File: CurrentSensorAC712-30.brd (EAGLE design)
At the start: 24 x 32 mm, 8 parts, among them U1 ACS712ELCTR30AT

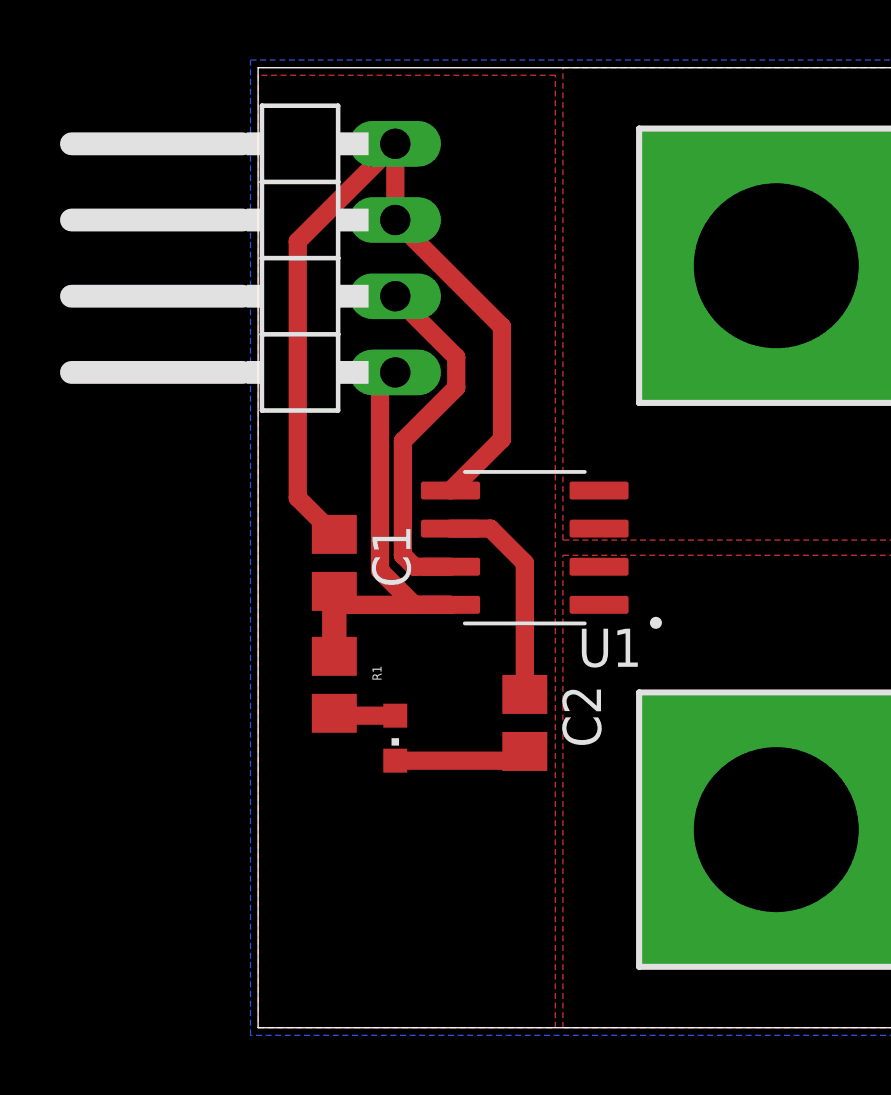
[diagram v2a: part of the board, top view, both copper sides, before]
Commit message: isolation distance improved
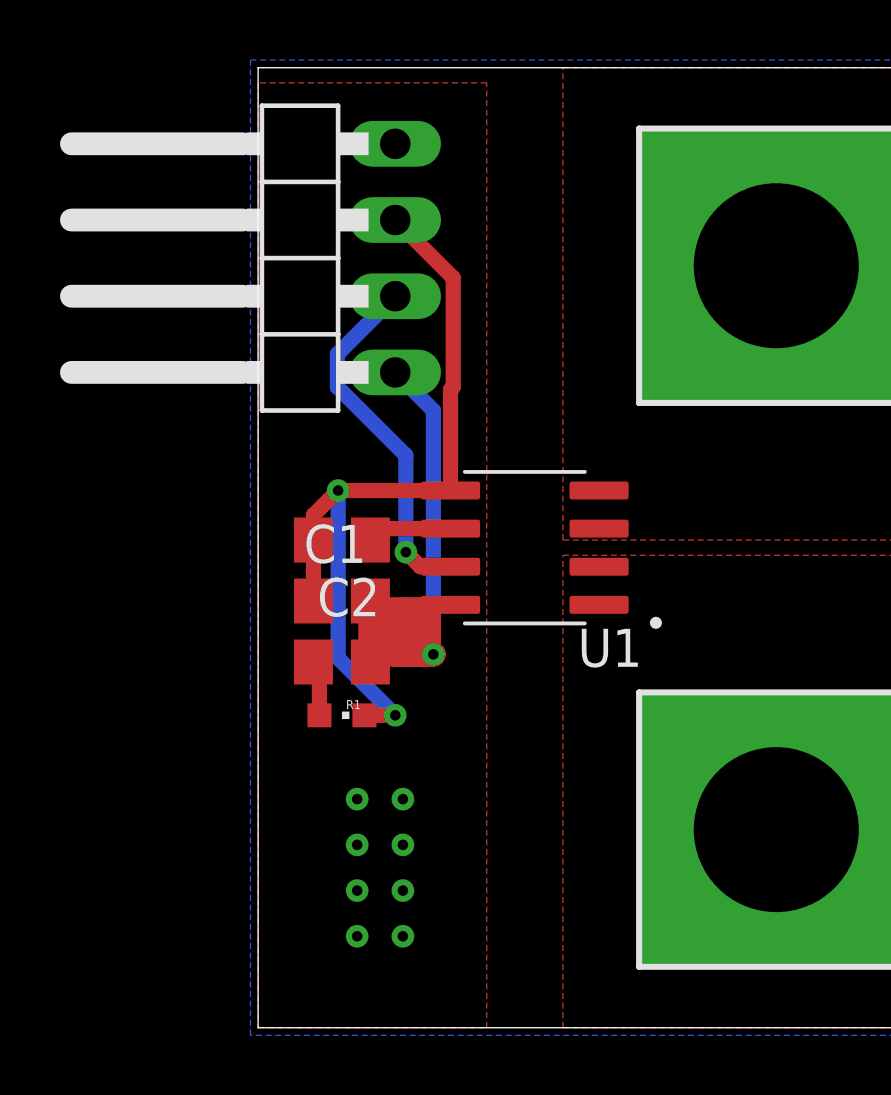
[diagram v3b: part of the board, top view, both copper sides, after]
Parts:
- moved C2 8.62 mm to (2.79, 16.3), turned to 180 degrees
- moved LED1 1.93 mm to (2.79, 10.4), turned to 270 degrees
- moved C1 1.30 mm to (2.79, 14.2), turned to 0 degrees
- moved R1 0.80 mm to (2.79, 12.2), turned to 180 degrees
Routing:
- net 5VDC: track 15.9 -> 33.3 mm, vias 0 -> 1
- net GND: track 33.1 -> 26.9 mm, vias 0 -> 10
- net N$4: track 7.33 -> 2.83 mm
- net N$6: vias 0 -> 1

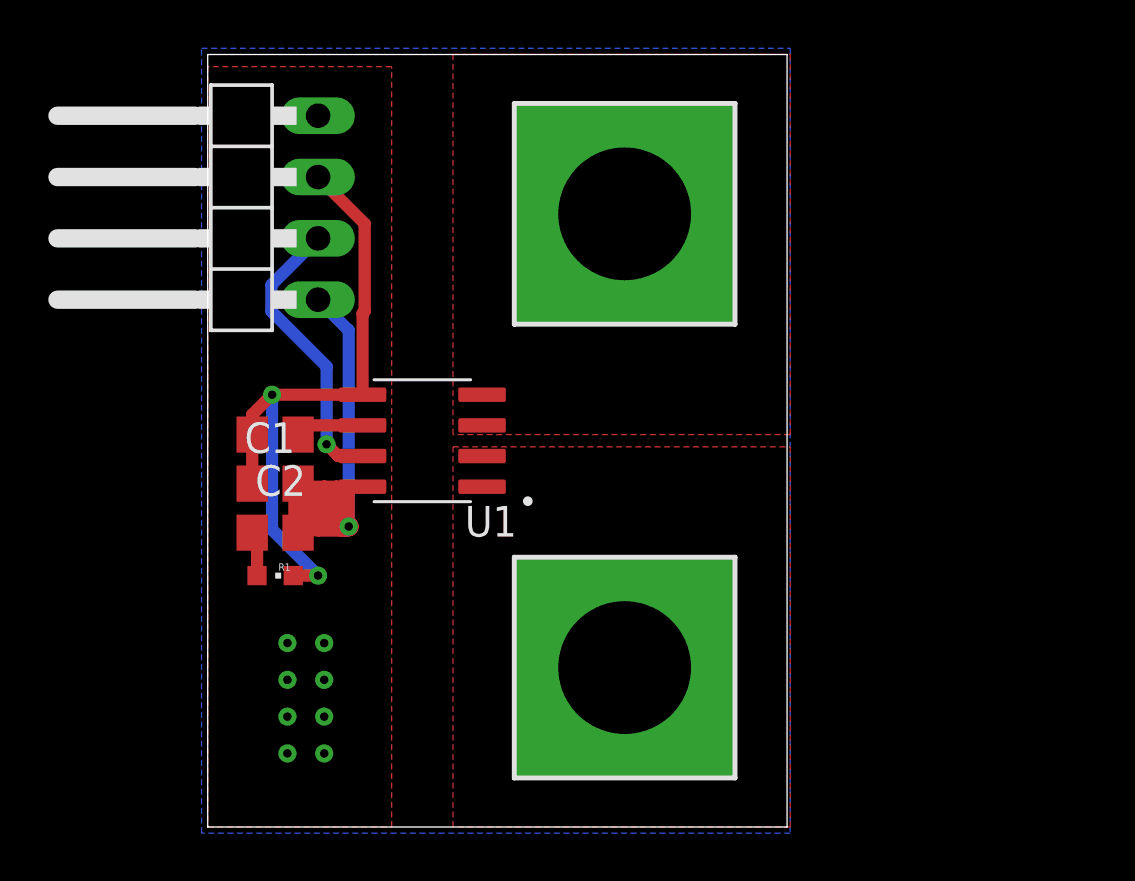
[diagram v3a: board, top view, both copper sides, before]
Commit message: new extension board design used
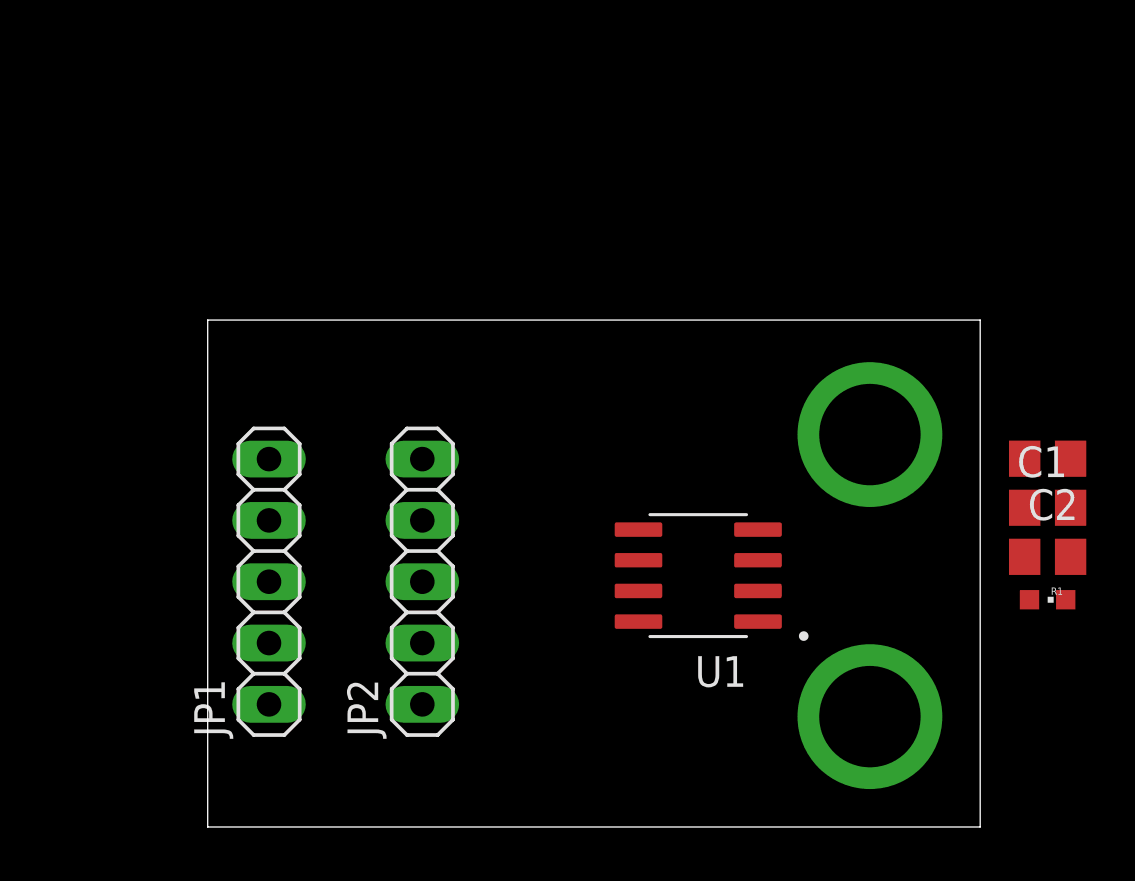
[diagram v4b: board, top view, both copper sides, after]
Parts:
- removed H1, H2: MOUNT-PAD-SQUARE5.5, holes:5,5-PAD-SQUARE
- added JP2: (no value), pinhead:1X05
- JP1: device pinhead:1X04/90 -> pinhead:1X05
- moved C1 32.0 mm to (34.8, 13.2)
- moved C2 32.0 mm to (34.8, 15.3)
- moved LED1 32.0 mm to (34.8, 9.41)
- moved R1 32.0 mm to (34.8, 11.2)
- moved JP1 15.6 mm to (2.54, 10.2)
- moved U1 12.7 mm to (20.3, 10.4)
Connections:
- net 5VDC: now also JP1.2
- net GND: now also JP1.5; no longer JP1.3
- net IN: no longer H1.B5,5
- net N$6: now also JP1.3; no longer JP1.2
- net OUT: no longer H2.B5,5
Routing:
- net 5VDC: track 33.3 -> 0.00 mm, vias 1 -> 0
- net GND: track 26.9 -> 0.00 mm, vias 10 -> 0
- net N$6: track 12.0 -> 0.00 mm, vias 1 -> 0
- net N$4: track 2.83 -> 0.00 mm
- net N$5: track 1.86 -> 0.00 mm
- removed copper zone on layer 1, net GND
- removed copper zone on layer 16, net GND
- removed copper zone on layer 1, net IN
- removed copper zone on layer 1, net OUT
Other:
- board size 24 x 32 mm -> 32 x 21 mm

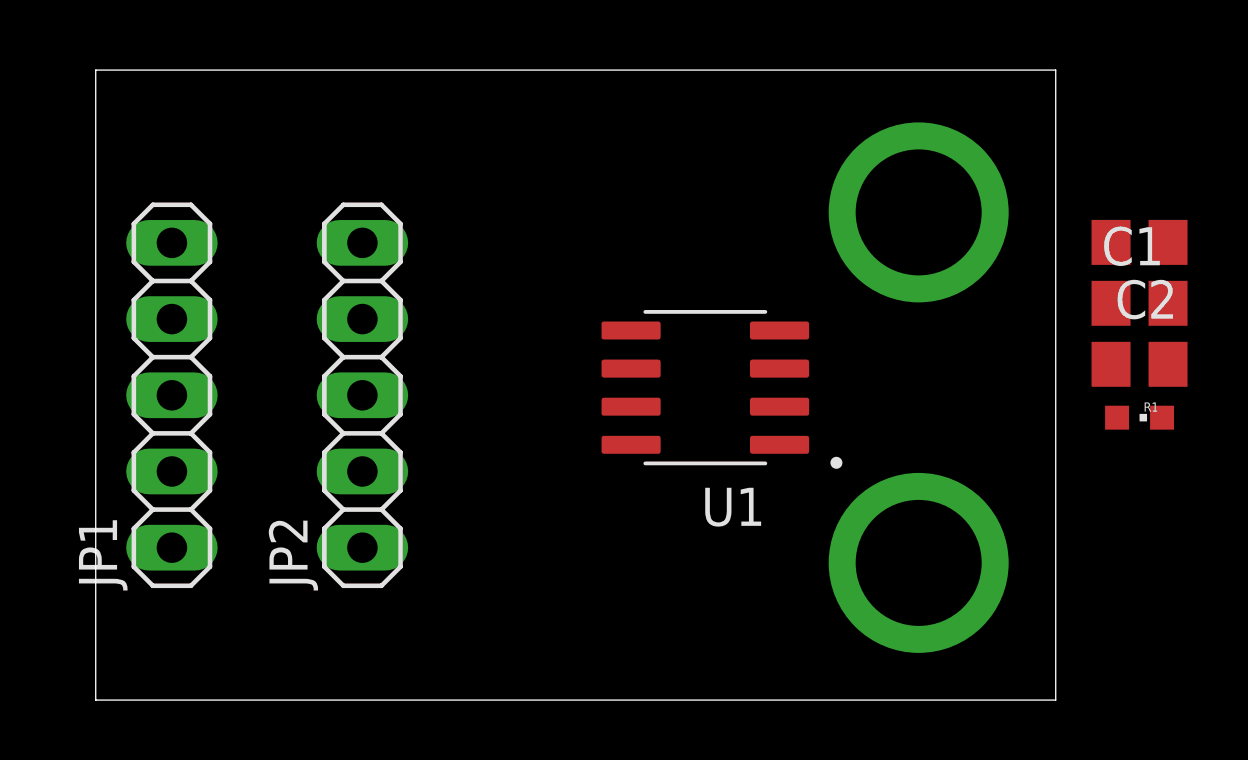
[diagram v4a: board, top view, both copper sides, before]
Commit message: current sensor board routed
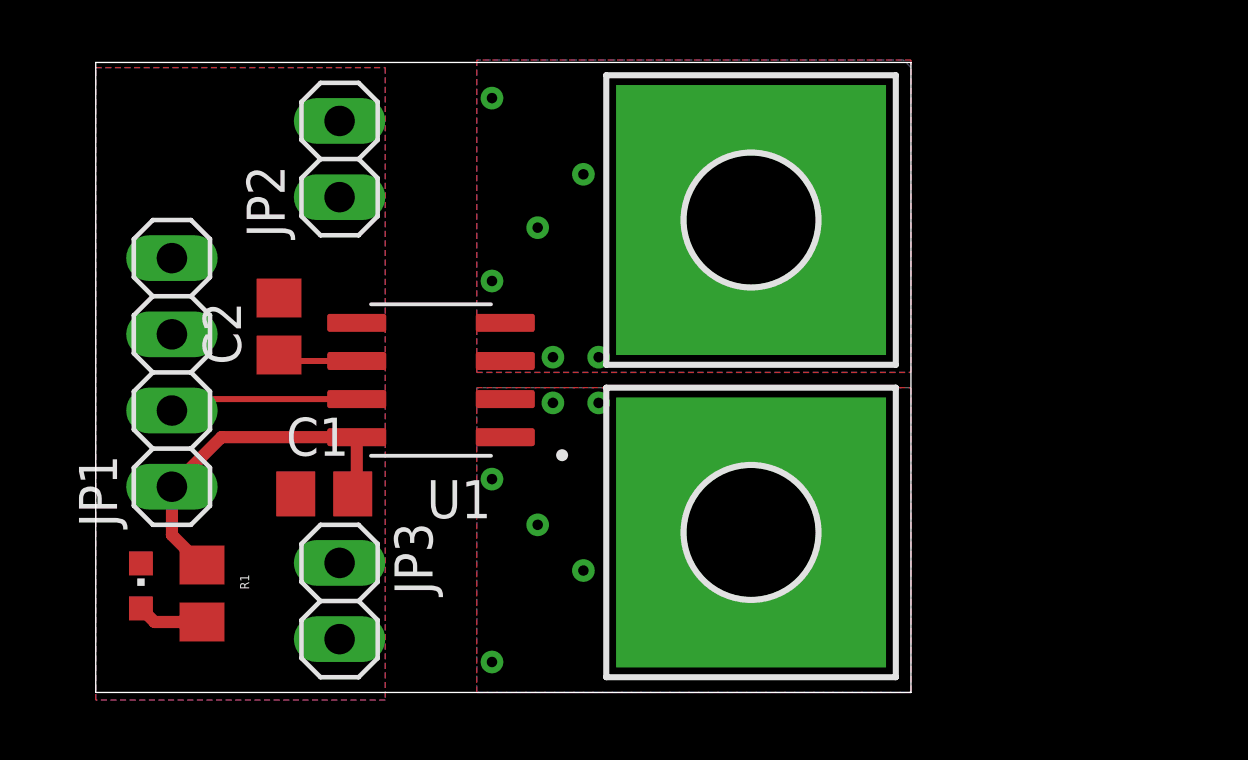
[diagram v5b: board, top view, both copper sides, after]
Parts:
- added H1, H2: MOUNT-PAD-SQUARE4.3, holes:4,3-PAD-SQUARE
- added JP3: (no value), pinhead:1X02
- JP1: device pinhead:1X05 -> pinhead:1X04
- JP2: device pinhead:1X05 -> pinhead:1X02
- moved LED1 33.8 mm to (1.51, 3.81), turned to 0 degrees
- moved R1 32.2 mm to (3.54, 3.55), turned to 270 degrees
- moved C2 28.8 mm to (6.11, 12.4), turned to 90 degrees
- moved C1 27.9 mm to (7.62, 6.87)
- moved U1 9.15 mm to (11.2, 10.7)
- moved JP2 7.91 mm to (8.13, 18.0)
- moved JP1 0.76 mm to (2.54, 10.9)
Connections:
- net 5VDC: no longer JP1.2
- net GND: now also JP1.3, JP2.1, JP2.2, JP3.1, JP3.2; no longer JP1.5
- net IN: now also H1.B4,3
- net N$6: now also JP1.2; no longer JP1.3
- net OUT: now also H2.B4,3
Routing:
- net 5VDC: track 0.00 -> 11.8 mm
- net N$6: track 0.00 -> 6.32 mm
- net N$4: track 0.00 -> 2.67 mm
- net N$5: track 0.00 -> 2.22 mm
- added copper zone on layer 1, net GND
- added copper zone on layer 16, net GND
- added copper zone on layer 1, net IN
- added copper zone on layer 16, net IN
- added copper zone on layer 1, net OUT
- added copper zone on layer 16, net OUT
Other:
- board size 32 x 21 mm -> 27.2 x 21 mm

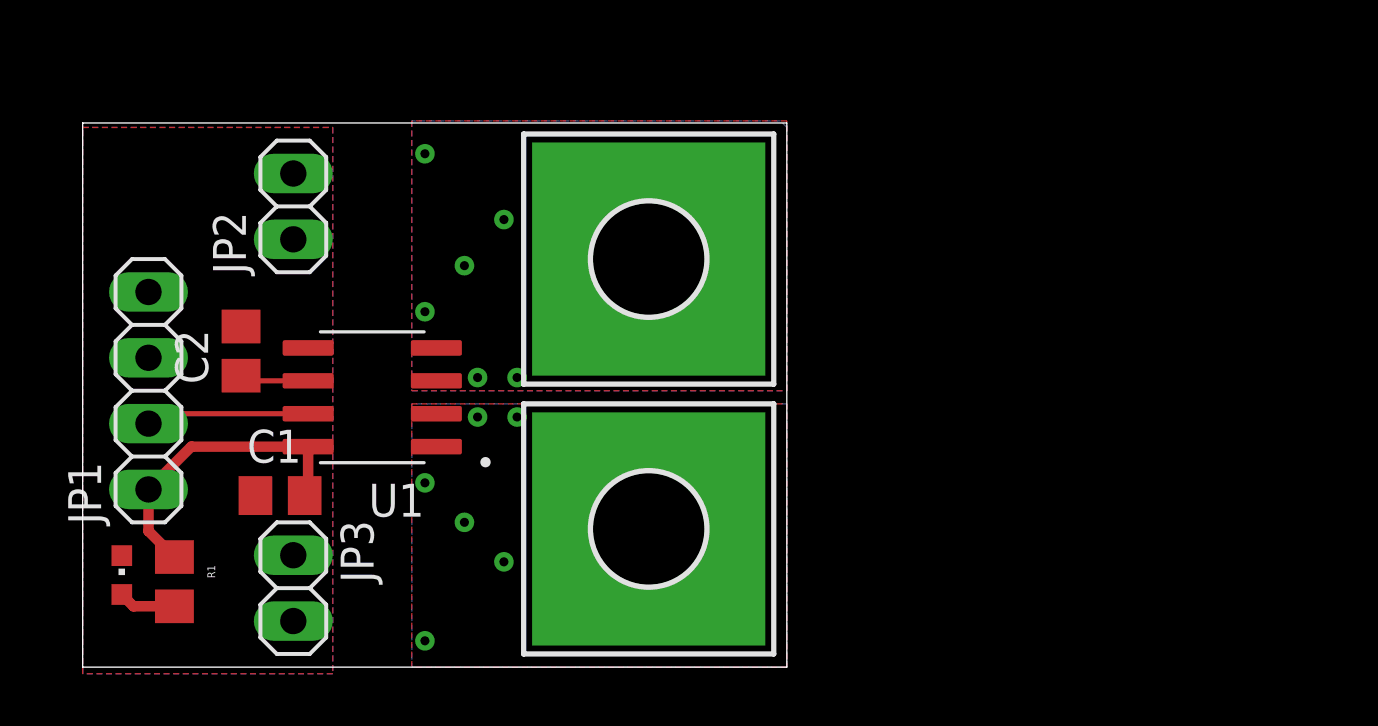
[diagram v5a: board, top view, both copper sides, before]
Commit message: sensor changed to ACS758
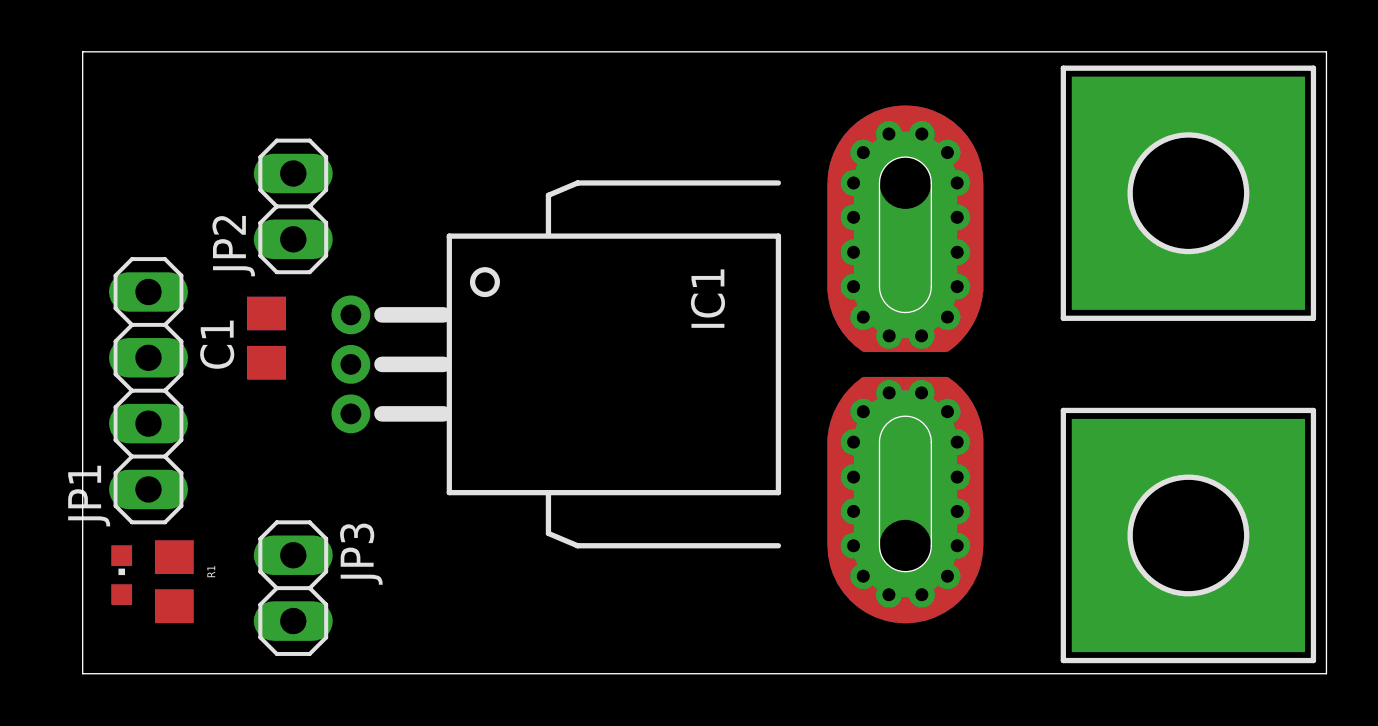
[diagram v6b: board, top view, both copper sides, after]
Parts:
- removed C2: 1nF, rcl:C0805
- removed U1: ACS712ELCTR30AT, ACS712ELCTR30AT:SOIC127P600X175-8N
- added IC1: ACS758LCB-050B-PFF-T, allegro-2:CB-PFF
- moved H2 21.0 mm to (42.7, 18.5)
- moved H1 20.8 mm to (42.7, 5.33)
- moved C1 6.10 mm to (7.10, 12.9), turned to 90 degrees
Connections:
- removed net N$4: C2.1, U1.6
- net 5VDC: now also IC1.1; no longer U1.8
- net GND: now also IC1.2; no longer C2.2, U1.5
- net IN: now also IC1.IP+, IC1.IP+@10, IC1.IP+@11, IC1.IP+@12, IC1.IP+@13, IC1.IP+@14, IC1.IP+@15, IC1.IP+@16, IC1.IP+@17, IC1.IP+@2, IC1.IP+@3, IC1.IP+@4, IC1.IP+@5, IC1.IP+@6, IC1.IP+@7, IC1.IP+@8, IC1.IP+@9; no longer U1.1, U1.2
- net N$6: now also IC1.3; no longer U1.7
- net OUT: now also IC1.IP-, IC1.IP-@10, IC1.IP-@11, IC1.IP-@12, IC1.IP-@13, IC1.IP-@14, IC1.IP-@15, IC1.IP-@16, IC1.IP-@17, IC1.IP-@2, IC1.IP-@3, IC1.IP-@4, IC1.IP-@5, IC1.IP-@6, IC1.IP-@7, IC1.IP-@8, IC1.IP-@9; no longer U1.3, U1.4
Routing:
- net 5VDC: track 11.8 -> 0.00 mm
- net N$6: track 6.32 -> 0.00 mm
- net N$4: track 2.67 -> 0.00 mm
- net N$5: track 2.22 -> 0.00 mm
- removed copper zone on layer 1, net GND
- removed copper zone on layer 16, net GND
- removed copper zone on layer 1, net IN
- removed copper zone on layer 16, net IN
- removed copper zone on layer 1, net OUT
- removed copper zone on layer 16, net OUT
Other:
- board size 27.2 x 21 mm -> 48 x 24 mm
